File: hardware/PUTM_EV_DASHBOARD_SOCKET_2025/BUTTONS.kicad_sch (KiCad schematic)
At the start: 12 parts, among them SW1 SW_Push, SW2 SW_Push, SW3 SW_Push, SW4 SW_Push, SW5 SW_Push, SW6 SW_Push

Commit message: prawie gotowe
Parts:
- removed R6: 1K, Resistor_SMD:R_1206_3216Metric, symbol Device:R_Small
- removed SW6: SW_Push, Button_Switch_SMD:SW_Push_1TS009xxxx-xxxx-xxxx_6x6x5mm, symbol Switch:SW_Push

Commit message: jest jako tako
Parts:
- SW1, SW2, SW3, SW4, SW5: footprint Button_Switch_SMD:SW_Push_1TS009xxxx-xxxx-xxxx_6x6x5mm -> Button_Switch_SMD:SW_Push_1P1T_NO_E-Switch_TL3301NxxxxxG
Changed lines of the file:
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@@
 		)
 	)
-	(global_label "BUTTON_4"
+	(hierarchical_label "BUTTON_2"
 		(shape input)
-		(at 147.32 95.25 0)
-		(fields_autoplaced yes)
+		(at 147.32 55.88 0)
 		(effects
 			(font
@@
 			(justify left)
 		)
-		(property "Intersheetrefs" "${INTERSHEET_REFS}"
-			(at 159.679 95.25 0)
-			(effects
-				(font
-					(size 1.27 1.27)
-				)
-				(justify left)
-				(hide yes)
-			)
-		)
-	)
-	(global_label "BUTTON_3"
+	)
+	(hierarchical_label "BUTTON_1"
 		(shape input)
-		(at 148.59 78.74 0)
-		(fields_autoplaced yes)
+		(at 146.05 33.02 0)
 		(effects
 			(font
@@
 			(justify left)
 		)
-		(property "Intersheetrefs" "${INTERSHEET_REFS}"
-			(at 160.949 78.74 0)
-			(effects
-				(font
-					(size 1.27 1.27)
-				)
-				(justify left)
-				(hide yes)
-			)
-		)
-	)
-	(global_label "BUTTON_5"
+	)
+	(hierarchical_label "BUTTON_3"
 		(shape input)
-		(at 148.59 118.11 0)
-		(fields_autoplaced yes)
+		(at 148.59 78.74 0)
 		(effects
 			(font
@@
 			(justify left)
 		)
-		(property "Intersheetrefs" "${INTERSHEET_REFS}"
-			(at 160.949 118.11 0)
-			(effects
-				(font
-					(size 1.27 1.27)
-				)
-				(justify left)
-				(hide yes)
-			)
-		)
-	)
-	(global_label "BUTTON_2"
+	)
+	(hierarchical_label "BUTTON_4"
 		(shape input)
-		(at 147.32 55.88 0)
-		(fields_autoplaced yes)
+		(at 147.32 95.25 0)
 		(effects
 			(font
@@
 			(justify left)
 		)
-		(property "Intersheetrefs" "${INTERSHEET_REFS}"
-			(at 159.679 55.88 0)
-			(effects
-				(font
-					(size 1.27 1.27)
-				)
-				(justify left)
-				(hide yes)
-			)
-		)
-	)
-	(global_label "BUTTON_1"
+	)
+	(hierarchical_label "BUTTON_5"
 		(shape input)
-		(at 146.05 33.02 0)
-		(fields_autoplaced yes)
+		(at 148.59 118.11 0)
 		(effects
 			(font
@@
 			(justify left)
 		)
-		(property "Intersheetrefs" "${INTERSHEET_REFS}"
-			(at 158.409 33.02 0)
-			(effects
-				(font
-					(size 1.27 1.27)
-				)
-				(justify left)
-				(hide yes)
-			)
-		)
 	)
 	(symbol
@@
 			)
 		)
-		(property "Footprint" "Button_Switch_SMD:SW_Push_1TS009xxxx-xxxx-xxxx_6x6x5mm"
+		(property "Footprint" "Button_Switch_SMD:SW_Push_1P1T_NO_E-Switch_TL3301NxxxxxG"
 			(at 133.35 27.94 0)
 			(effects
@@
 			)
 		)
-		(property "Footprint" "Button_Switch_SMD:SW_Push_1TS009xxxx-xxxx-xxxx_6x6x5mm"
+		(property "Footprint" "Button_Switch_SMD:SW_Push_1P1T_NO_E-Switch_TL3301NxxxxxG"
 			(at 134.62 90.17 0)
 			(effects
@@
 			)
 		)
-		(property "Footprint" "Button_Switch_SMD:SW_Push_1TS009xxxx-xxxx-xxxx_6x6x5mm"
+		(property "Footprint" "Button_Switch_SMD:SW_Push_1P1T_NO_E-Switch_TL3301NxxxxxG"
 			(at 135.89 73.66 0)
 			(effects
@@
 			)
 		)
-		(property "Footprint" "Button_Switch_SMD:SW_Push_1TS009xxxx-xxxx-xxxx_6x6x5mm"
+		(property "Footprint" "Button_Switch_SMD:SW_Push_1P1T_NO_E-Switch_TL3301NxxxxxG"
 			(at 135.89 113.03 0)
 			(effects
@@
 			)
 		)
-		(property "Footprint" "Button_Switch_SMD:SW_Push_1TS009xxxx-xxxx-xxxx_6x6x5mm"
+		(property "Footprint" "Button_Switch_SMD:SW_Push_1P1T_NO_E-Switch_TL3301NxxxxxG"
 			(at 134.62 50.8 0)
 			(effects

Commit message: g3
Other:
- note added: "PRZYCISKI"
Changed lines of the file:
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@@
 	(generator_version "9.0")
 	(paper "A4")
+	(rectangle
+		(start 113.665 16.51)
+		(end 167.005 138.43)
+		(stroke
+			(width 0)
+			(type default)
+		)
+		(fill
+			(type none)
+		)
+	)
+	(text "PRZYCISKI\n"
+		(exclude_from_sim no)
+		(at 122.682 19.812 0)
+		(effects
+			(font
+				(size 1.27 1.27)
+			)
+		)
+	)
 	(junction
 		(at 139.7 55.88)

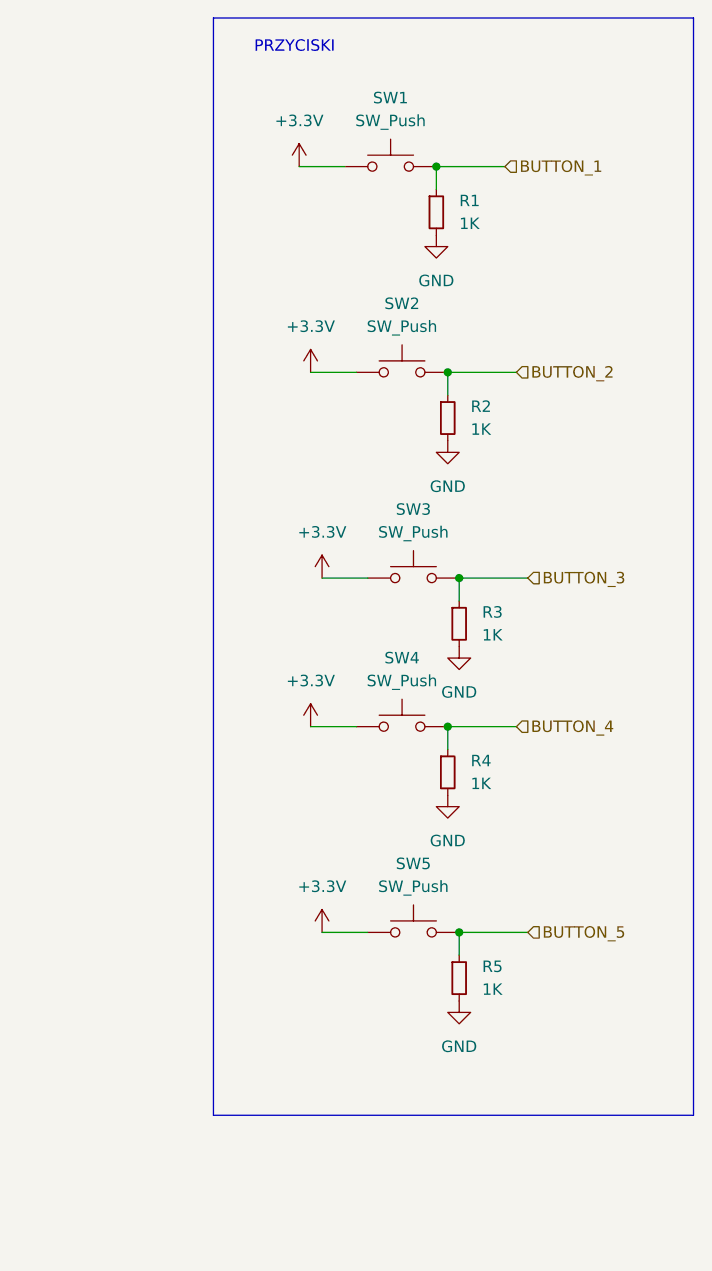
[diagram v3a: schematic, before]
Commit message: fixed button logic, holes for inserts, distance from mounting holes to P4 socket, changed jumpers, TVS diode and footprint for laboratory socket 4m
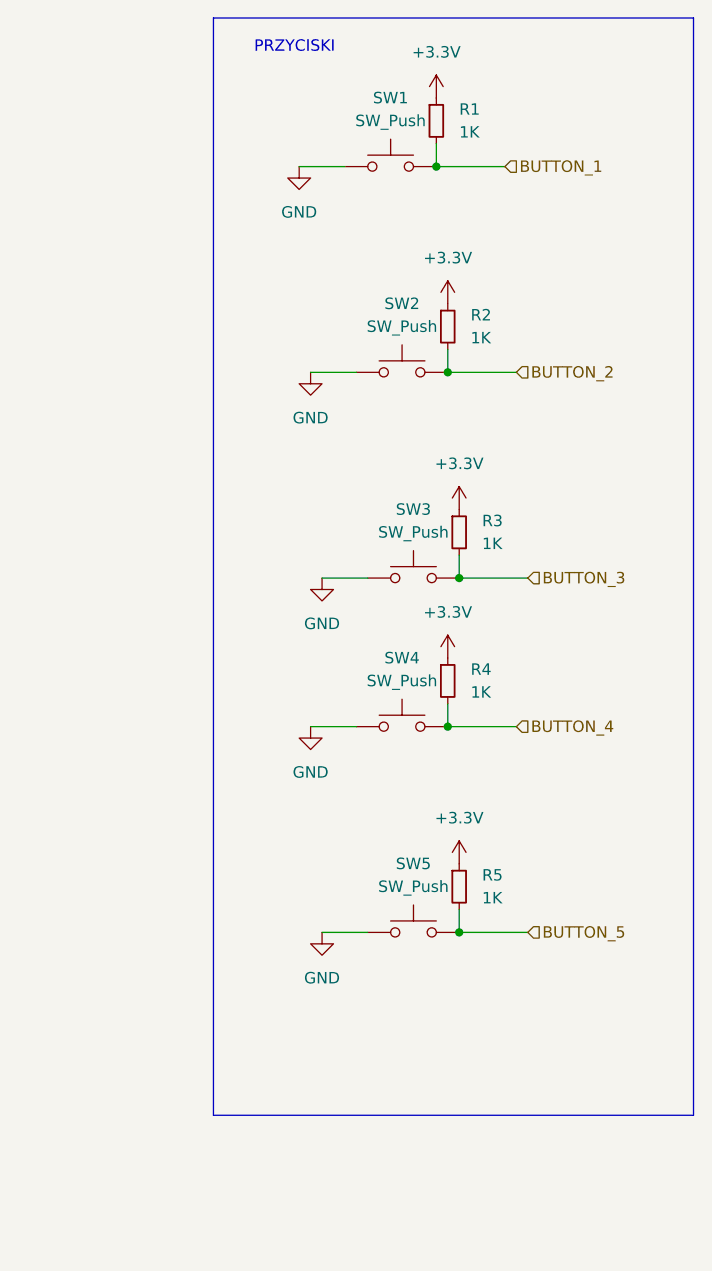
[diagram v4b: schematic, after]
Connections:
- net +3.3V: now also R1.1, R2.1, R3.1, R4.1, R5.1; no longer SW1.1, SW2.1, SW3.1, SW4.1, SW5.1
- net BUTTON_1: now also R1.2; no longer R1.1
- net BUTTON_2: now also R2.2; no longer R2.1
- net BUTTON_3: now also R3.2; no longer R3.1
- net BUTTON_4: now also R4.2; no longer R4.1
- net BUTTON_5: now also R5.2; no longer R5.1
- net GND: now also SW1.1, SW2.1, SW3.1, SW4.1, SW5.1; no longer R1.2, R2.2, R3.2, R4.2, R5.2
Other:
- moved on the sheet: R1, R2, R3, R4, R5

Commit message: fixed layout
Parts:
- removed SW1, SW2, SW3, SW4, SW5: SW_Push, Button_Switch_SMD:SW_Push_1P1T_NO_E-Switch_TL3301NxxxxxG, symbol Switch:SW_Push
- added S1, S2, S3, S4, S5: PTS526SM15SMTR2_LFS, PTS526SM15SMTR2LFS, symbol SamacSys_Parts:PTS526SM15SMTR2_LFS
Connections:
- net BUTTON_1: now also S1.3 (NO_1), S1.4 (NO_2)
- net BUTTON_2: now also S2.3 (NO_1), S2.4 (NO_2)
- net BUTTON_3: now also S4.3 (NO_1), S4.4 (NO_2)
- net BUTTON_4: now also S3.3 (NO_1), S3.4 (NO_2)
- net BUTTON_5: now also S5.3 (NO_1), S5.4 (NO_2)
- net GND: now also S1.1 (COM_1), S1.2 (COM_2), S2.1 (COM_1), S2.2 (COM_2), S3.1 (COM_1), S3.2 (COM_2), S4.1 (COM_1), S4.2 (COM_2), S5.1 (COM_1), S5.2 (COM_2)
